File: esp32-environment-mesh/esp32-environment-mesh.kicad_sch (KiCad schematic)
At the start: 7 parts, among them J1 USB_B_Micro, SW1 SW_Push_LED, U1 ESP32-C3-WROOM-02

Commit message: updated schematic
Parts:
- removed D2: LED, LED_SMD:LED_1206_3216Metric_Pad1.42x1.75mm_HandSolder, symbol Device:LED
- added J2: T6793, custom-parts:T6793, symbol custom-parts:T6793
- added U3: LM2576S-5, Package_TO_SOT_SMD:TO-263-5_TabPin3, symbol Regulator_Switching:LM2576S-5
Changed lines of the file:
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@@
-	(symbol
-		(lib_id "Device:LED")
-		(at 170.18 26.67 0)
-		(unit 1)
-		(exclude_from_sim no)
-		(in_bom yes)
-		(on_board yes)
-		(dnp no)
-		(fields_autoplaced yes)
-		(property "Reference" "D2"
-			(at 168.5925 20.32 0)
-			(effects
-				(font
-					(size 1.27 1.27)
-				)
-			)
-		)
-		(property "Value" "LED"
-			(at 168.5925 22.86 0)
-			(effects
-				(font
-					(size 1.27 1.27)
-				)
-			)
-		)
-		(property "Footprint" "LED_SMD:LED_1206_3216Metric_Pad1.42x1.75mm_HandSolder"
-			(at 170.18 26.67 0)
-			(effects
-				(font
-					(size 1.27 1.27)
-				)
-				(hide yes)
-			)
-		)
-		(property "Datasheet" "~"
-			(at 170.18 26.67 0)
-			(effects
-				(font
-					(size 1.27 1.27)
-				)
-				(hide yes)
-			)
-		)
-		(property "Description" "Light emitting diode"
-			(at 170.18 26.67 0)
-			(effects
-				(font
-					(size 1.27 1.27)
-				)
-				(hide yes)
-			)
-		)
-		(property "Sim.Pins" "1=K 2=A"
-			(at 170.18 26.67 0)
-			(effects
-				(font
-					(size 1.27 1.27)
-				)
-				(hide yes)
-			)
-		)
-		(pin "1"
-		)
-		(pin "2"
-		)
-		(instances
-			(project "esp32-environment-mesh"
-				(path "/627e545e-09a0-4c83-8f4f-f7952e619641"
-					(reference "D2")
-					(unit 1)
-				)
-			)
-		)
-	)
 	(symbol
 		(lib_id "Device:LED")
@@
 	)
 	(symbol
+		(lib_id "custom-parts:T6793")
+		(at 143.51 134.62 0)
+		(unit 1)
+		(exclude_from_sim no)
+		(in_bom yes)
+		(on_board yes)
+		(dnp no)
+		(fields_autoplaced yes)
+		(property "Reference" "J2"
+			(at 200.66 127 0)
+			(effects
+				(font
+					(size 1.27 1.27)
+				)
+			)
+		)
+		(property "Value" "T6793"
+			(at 200.66 129.54 0)
+			(effects
+				(font
+					(size 1.27 1.27)
+				)
+			)
+		)
+		(property "Footprint" "custom-parts:T6793"
+			(at 254 229.54 0)
+			(effects
+				(font
+					(size 1.27 1.27)
+				)
+				(justify left top)
+				(hide yes)
+			)
+		)
+		(property "Datasheet" ""
+			(at 254 329.54 0)
+			(effects
+				(font
+					(size 1.27 1.27)
+				)
+				(justify left top)
+				(hide yes)
+			)
+		)
+		(property "Description" "Air Quality Sensors T6793 NDIR CO2 Module 0-2K PPM"
+			(at 175.768 130.048 0)
+			(effects
+				(font
+					(size 1.27 1.27)
+				)
+				(hide yes)
+			)
+		)
+		(property "Height" "8.61"
+			(at 254 529.54 0)
+			(effects
+				(font
+					(size 1.27 1.27)
+				)
+				(justify left top)
+				(hide yes)
+			)
+		)
+		(property "Mouser Part Number" "527-T6793"
+			(at 254 629.54 0)
+			(effects
+				(font
+					(size 1.27 1.27)
+				)
+				(justify left top)
+				(hide yes)
+			)
+		)
+		(property "Mouser Price/Stock" "https://www.mouser.co.uk/ProductDetail/Amphenol-Advanced-Sensors/T6793?qs=doiCPypUmgEWnHL00v9AUQ%3D%3D"
+			(at 254 729.54 0)
+			(effects
+				(font
+					(size 1.27 1.27)
+				)
+				(justify left top)
+				(hide yes)
+			)
+		)
+		(property "Manufacturer_Name" "Amphenol"
+			(at 254 829.54 0)
+			(effects
+				(font
+					(size 1.27 1.27)
+				)
+				(justify left top)
+				(hide yes)
+			)
+		)
+		(property "Manufacturer_Part_Number" "T6793"
+			(at 254 929.54 0)
+			(effects
+				(font
+					(size 1.27 1.27)
+				)
+				(justify left top)
+				(hide yes)
+			)
+		)
+		(pin "1"
+		)
+		(pin "2"
+		)
+		(pin "5"
+		)
+		(pin "6"
+		)
+		(pin "4"
+		)
+		(pin "3"
+		)
+		(instances
+			(project ""
+				(path "/627e545e-09a0-4c83-8f4f-f7952e619641"
+					(reference "J2")
+					(unit 1)
+				)
+			)
+		)
+	)
+	(symbol
 		(lib_id "Switch:SW_Push_LED")
 		(at 138.43 45.72 0)
@@
 					(unit 1)
 				)
+			)
+		)
+	)
+	(symbol
+		(lib_id "Regulator_Switching:LM2576S-5")
+		(at 88.9 38.1 0)
+		(unit 1)
+		(exclude_from_sim no)
+		(in_bom yes)
+		(on_board yes)
+		(dnp no)
+		(fields_autoplaced yes)
+		(property "Reference" "U3"
+			(at 88.9 27.94 0)
+			(effects
+				(font
+					(size 1.27 1.27)
+				)
+			)
+		)
+		(property "Value" "LM2576S-5"
+			(at 88.9 30.48 0)
+			(effects
+				(font
+					(size 1.27 1.27)
+				)
+			)
+		)
+		(property "Footprint" "Package_TO_SOT_SMD:TO-263-5_TabPin3"
+			(at 88.9 44.45 0)
+			(effects
+				(font
+					(size 1.27 1.27)
+					(italic yes)
+				)
+				(justify left)
+				(hide yes)
+			)
+		)
+		(property "Datasheet" "http://www.ti.com/lit/ds/symlink/lm2576.pdf"
+			(at 88.9 38.1 0)
+			(effects
+				(font
+					(size 1.27 1.27)
+				)
+				(hide yes)
+			)
+		)
+		(property "Description" "5V, 3A SIMPLE SWITCHER® Step-Down Voltage Regulator, TO-263"
+			(at 88.9 38.1 0)
+			(effects
+				(font
+					(size 1.27 1.27)
+				)
+				(hide yes)
+			)
+		)
+		(pin "3"
+		)
+		(pin "4"
+		)
+		(pin "5"
+		)
+		(pin "2"
+		)
+		(pin "1"
+		)
+		(instances
+			(project ""
+				(path "/627e545e-09a0-4c83-8f4f-f7952e619641"
+					(reference "U3")
+					(unit 1)
+				)

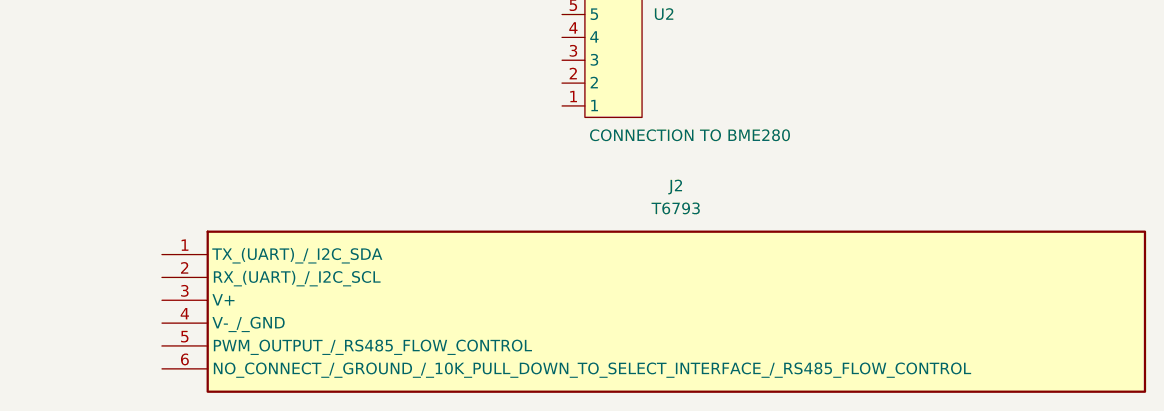
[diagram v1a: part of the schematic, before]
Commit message: Update esp32-environment-mesh.kicad_sch
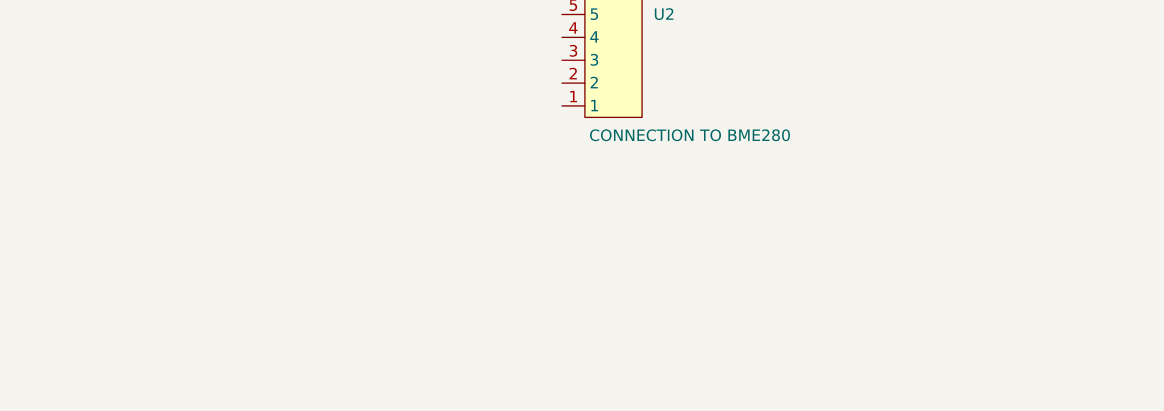
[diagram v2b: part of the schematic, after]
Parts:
- removed J2: T6793, custom-parts:T6793, symbol custom-parts:T6793
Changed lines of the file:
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@@
-	)
-	(symbol
-		(lib_id "custom-parts:T6793")
-		(at 143.51 134.62 0)
-		(unit 1)
-		(exclude_from_sim no)
-		(in_bom yes)
-		(on_board yes)
-		(dnp no)
-		(fields_autoplaced yes)
-		(property "Reference" "J2"
-			(at 200.66 127 0)
-			(effects
-				(font
-					(size 1.27 1.27)
-				)
-			)
-		)
-		(property "Value" "T6793"
-			(at 200.66 129.54 0)
-			(effects
-				(font
-					(size 1.27 1.27)
-				)
-			)
-		)
-		(property "Footprint" "custom-parts:T6793"
-			(at 254 229.54 0)
-			(effects
-				(font
-					(size 1.27 1.27)
-				)
-				(justify left top)
-				(hide yes)
-			)
-		)
-		(property "Datasheet" ""
-			(at 254 329.54 0)
-			(effects
-				(font
-					(size 1.27 1.27)
-				)
-				(justify left top)
-				(hide yes)
-			)
-		)
-		(property "Description" "Air Quality Sensors T6793 NDIR CO2 Module 0-2K PPM"
-			(at 175.768 130.048 0)
-			(effects
-				(font
-					(size 1.27 1.27)
-				)
-				(hide yes)
-			)
-		)
-		(property "Height" "8.61"
-			(at 254 529.54 0)
-			(effects
-				(font
-					(size 1.27 1.27)
-				)
-				(justify left top)
-				(hide yes)
-			)
-		)
-		(property "Mouser Part Number" "527-T6793"
-			(at 254 629.54 0)
-			(effects
-				(font
-					(size 1.27 1.27)
-				)
-				(justify left top)
-				(hide yes)
-			)
-		)
-		(property "Mouser Price/Stock" "https://www.mouser.co.uk/ProductDetail/Amphenol-Advanced-Sensors/T6793?qs=doiCPypUmgEWnHL00v9AUQ%3D%3D"
-			(at 254 729.54 0)
-			(effects
-				(font
-					(size 1.27 1.27)
-				)
-				(justify left top)
-				(hide yes)
-			)
-		)
-		(property "Manufacturer_Name" "Amphenol"
-			(at 254 829.54 0)
-			(effects
-				(font
-					(size 1.27 1.27)
-				)
-				(justify left top)
-				(hide yes)
-			)
-		)
-		(property "Manufacturer_Part_Number" "T6793"
-			(at 254 929.54 0)
-			(effects
-				(font
-					(size 1.27 1.27)
-				)
-				(justify left top)
-				(hide yes)
-			)
-		)
-		(pin "1"
-		)
-		(pin "2"
-		)
-		(pin "5"
-		)
-		(pin "6"
-		)
-		(pin "4"
-		)
-		(pin "3"
-		)
-		(instances
-			(project ""
-				(path "/627e545e-09a0-4c83-8f4f-f7952e619641"
-					(reference "J2")
-					(unit 1)
-				)
-			)
-		)
 	)
 	(symbol
